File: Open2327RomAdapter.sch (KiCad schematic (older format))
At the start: 7 parts, among them P1 Conn_01x04, P99 OSHW_LOGO, U1 2364, U2 27128

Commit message: Fix ERC
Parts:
- U1: value 2364 -> 2364_SOCKET
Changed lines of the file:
@@
 Title "Open2327RomAdapter: C64 ROM 24 -> EPROM 28 Pin Adapter"
 Date "2018-01-05"
-Rev "2"
+Rev "3"
 Comp "SukkoPera"
 Comment1 "https://ist.uwaterloo.ca/~~schepers/sockets.html"
@@
 	1    0    0    -1
 $EndComp
-$Comp
-L power:GND #PWR05
-U 1 1 596BE63E
-P 10500 1000
-F 0 "#PWR05" H 10500 750 50  0001 C CNN
-F 1 "GND" H 10500 850 50  0000 C CNN
-F 2 "" H 10500 1000 50  0000 C CNN
-F 3 "" H 10500 1000 50  0000 C CNN
-	1    10500 1000
-	1    0    0    -1
-$EndComp
-$Comp
-L power:VCC #PWR06
-U 1 1 596BE658
-P 9900 900
-F 0 "#PWR06" H 9900 750 50  0001 C CNN
-F 1 "VCC" H 9900 1050 50  0000 C CNN
-F 2 "" H 9900 900 50  0000 C CNN
-F 3 "" H 9900 900 50  0000 C CNN
-	1    9900 900
-	1    0    0    -1
-$EndComp
-$Comp
-L power:PWR_FLAG #FLG07
-U 1 1 596BE672
-P 10500 900
-F 0 "#FLG07" H 10500 995 50  0001 C CNN
-F 1 "PWR_FLAG" H 10500 1080 50  0000 C CNN
-F 2 "" H 10500 900 50  0000 C CNN
-F 3 "" H 10500 900 50  0000 C CNN
-	1    10500 900
-	1    0    0    -1
-$EndComp
-$Comp
-L power:PWR_FLAG #FLG08
-U 1 1 596BE6A2
-P 9900 1000
-F 0 "#FLG08" H 9900 1095 50  0001 C CNN
-F 1 "PWR_FLAG" H 9900 1180 50  0000 C CNN
-F 2 "" H 9900 1000 50  0000 C CNN
-F 3 "" H 9900 1000 50  0000 C CNN
-	1    9900 1000
-	-1   0    0    1
-$EndComp
 Wire Wire Line
 	4950 4400 2850 4400
@@
 Wire Wire Line
 	3550 2600 3550 2650
-Wire Wire Line
-	9900 900  9900 1000
-Wire Wire Line
-	10500 900  10500 1000
 Wire Wire Line
 	4250 2450 4400 2450
@@
 P 5400 4950
 F 0 "U1" H 5590 5650 50  0000 C CNN
-F 1 "2364" H 5550 4245 50  0000 C CNN
+F 1 "2364_SOCKET" H 5550 4245 50  0000 C CNN
 F 2 "Open2327RomAdapter:DIP-24_W15.24mm-Notch" H 5400 4950 50  0001 C CNN
 F 3 "DOCUMENTATION" H 5400 4950 50  0001 C CNN

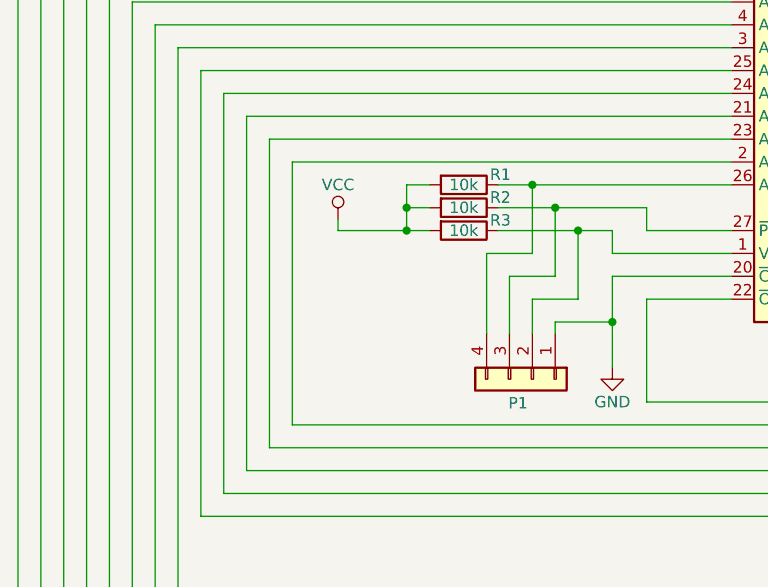
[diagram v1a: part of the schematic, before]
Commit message: Add jumper, pull-up and pad so that A12 can optionally be driven externally
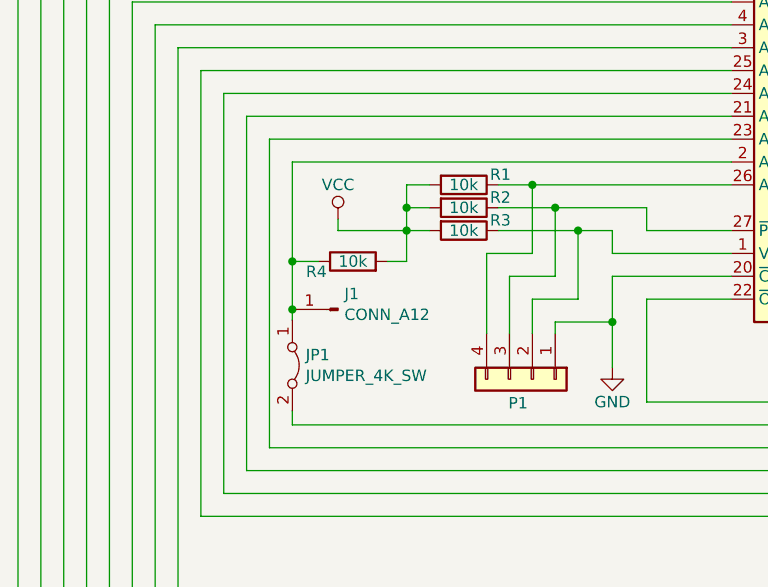
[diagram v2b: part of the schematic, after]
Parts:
- added J1: CONN_A12, TestPoint:TestPoint_Pad_D1.0mm, symbol Connector:Conn_01x01_Male
- added JP1: JUMPER_4K_SW, Jumper:SolderJumper-2_P1.3mm_Bridged_RoundedPad1.0x1.5mm, symbol Jumper:Jumper_2_Bridged
- added R4: 10k, Resistor_SMD:R_0805_2012Metric_Pad1.15x1.40mm_HandSolder, symbol Device:R
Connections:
- net VCC: now also R4.2
- net at U2.2 (A12): now also J1.1 (Pin_1), JP1.1 (A), R4.1; no longer U1.21 (A12)
- new net: JP1.2 (B), U1.21 (A12)
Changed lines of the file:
@@
 EESchema Schematic File Version 4
-LIBS:Open2327RomAdapter-cache
-EELAYER 26 0
+EELAYER 30 0
 EELAYER END
 $Descr A4 11693 8268
@@
 Sheet 1 1
 Title "Open2327RomAdapter: C64 ROM 24 -> EPROM 28 Pin Adapter"
-Date "2018-01-05"
+Date "2020-04-16"
 Rev "3"
 Comp "SukkoPera"
@@
 	5270 2350 3350 2350
 Wire Wire Line
-	3350 2350 3350 3500
-Wire Wire Line
 	3350 3500 6300 3500
 Wire Wire Line
@@
 $EndComp
 NoConn ~ 10890 6245
+Wire Wire Line
+	3350 3440 3350 3500
+$Comp
+L Jumper:Jumper_2_Bridged JP1
+U 1 1 5E98DDF8
+P 3350 3240
+F 0 "JP1" V 3304 3298 50  0000 L CNN
+F 1 "JUMPER_4K_SW" V 3395 3298 50  0000 L CNN
+F 2 "Jumper:SolderJumper-2_P1.3mm_Bridged_RoundedPad1.0x1.5mm" H 3350 3240 50  0001 C CNN
+F 3 "~" H 3350 3240 50  0001 C CNN
+	1    3350 3240
+	0    1    1    0
+$EndComp
+$Comp
+L Connector:Conn_01x01_Male J1
+U 1 1 5E9A2BF5
+P 3550 2995
+F 0 "J1" H 3522 2927 50  0000 R CNN
+F 1 "CONN_A12" H 3522 3018 50  0000 R CNN
+F 2 "TestPoint:TestPoint_Pad_D1.0mm" H 3550 2995 50  0001 C CNN
+F 3 "~" H 3550 2995 50  0001 C CNN
+	1    3550 2995
+	-1   0    0    1
+$EndComp
+$Comp
+L Device:R R4
+U 1 1 5E9B71C8
+P 3615 2785
+F 0 "R4" V 3570 2945 50  0000 C CNN
+F 1 "10k" V 3615 2785 50  0000 C CNN
+F 2 "Resistor_SMD:R_0805_2012Metric_Pad1.15x1.40mm_HandSolder" V 3545 2785 50  0001 C CNN
+F 3 "~" H 3615 2785 50  0001 C CNN
+	1    3615 2785
+	0    -1   -1   0
+$EndComp
+Wire Wire Line
+	3350 2350 3350 2785
+Wire Wire Line
+	3465 2785 3350 2785
+Connection ~ 3350 2785
+Wire Wire Line
+	3350 2785 3350 2995
+Wire Wire Line
+	3765 2785 3850 2785
+Wire Wire Line
+	3850 2785 3850 2650
+Connection ~ 3350 2995
+Wire Wire Line
+	3350 2995 3350 3040
 $EndSCHEMATC
